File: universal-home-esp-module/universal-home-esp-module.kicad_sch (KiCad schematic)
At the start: 12 parts, among them J1 ES8311 CODEC, J10 ESP32_RPINS, J2 LDR MOD, J3 RELAYS, J4 RGB LED, J5 ENV SENSOR, J6 5V PWR, J7 EXT_GPIO, J8 EXT_I2C, J9 ESP32_LPINS, U1 ESP32-C3_SUPERMINI_SMD, U2 74HC595

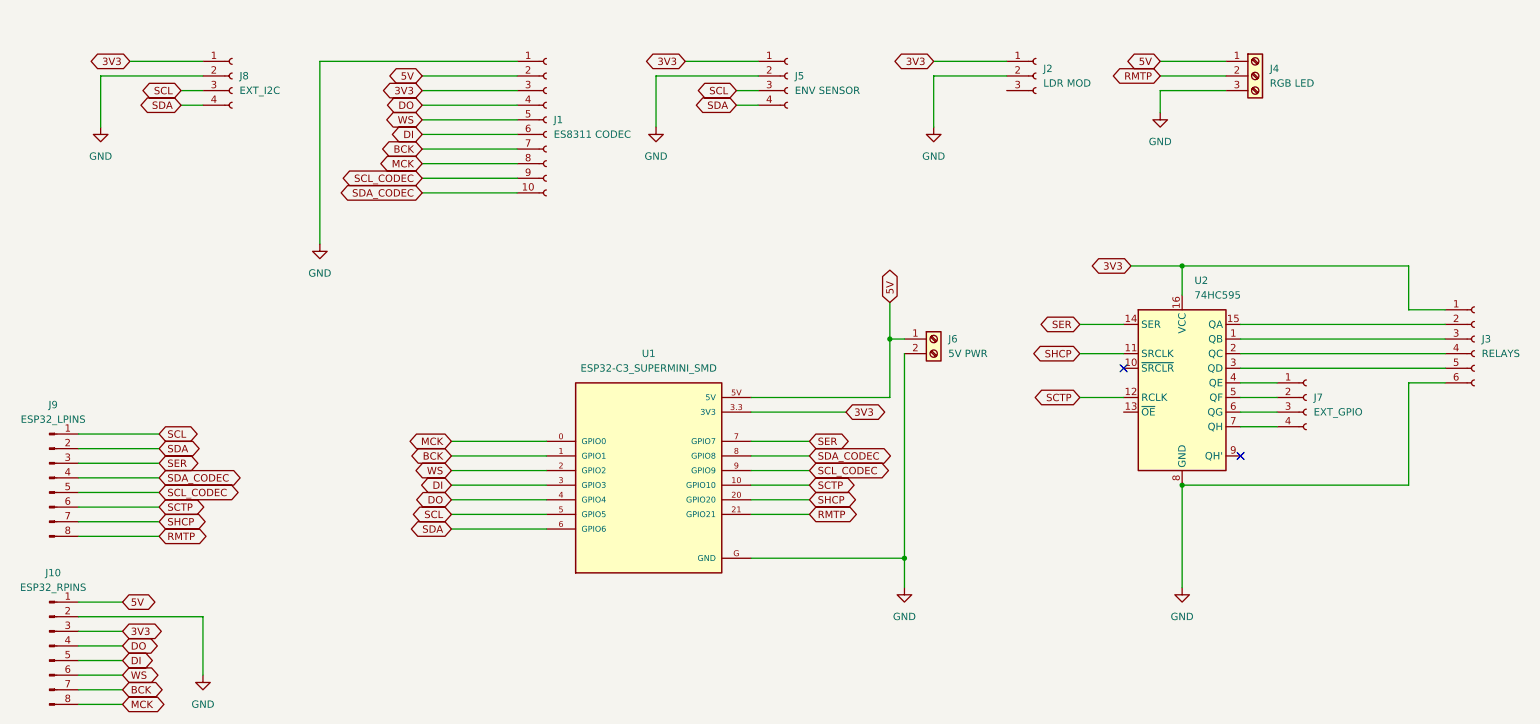
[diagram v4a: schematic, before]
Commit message: update schematic
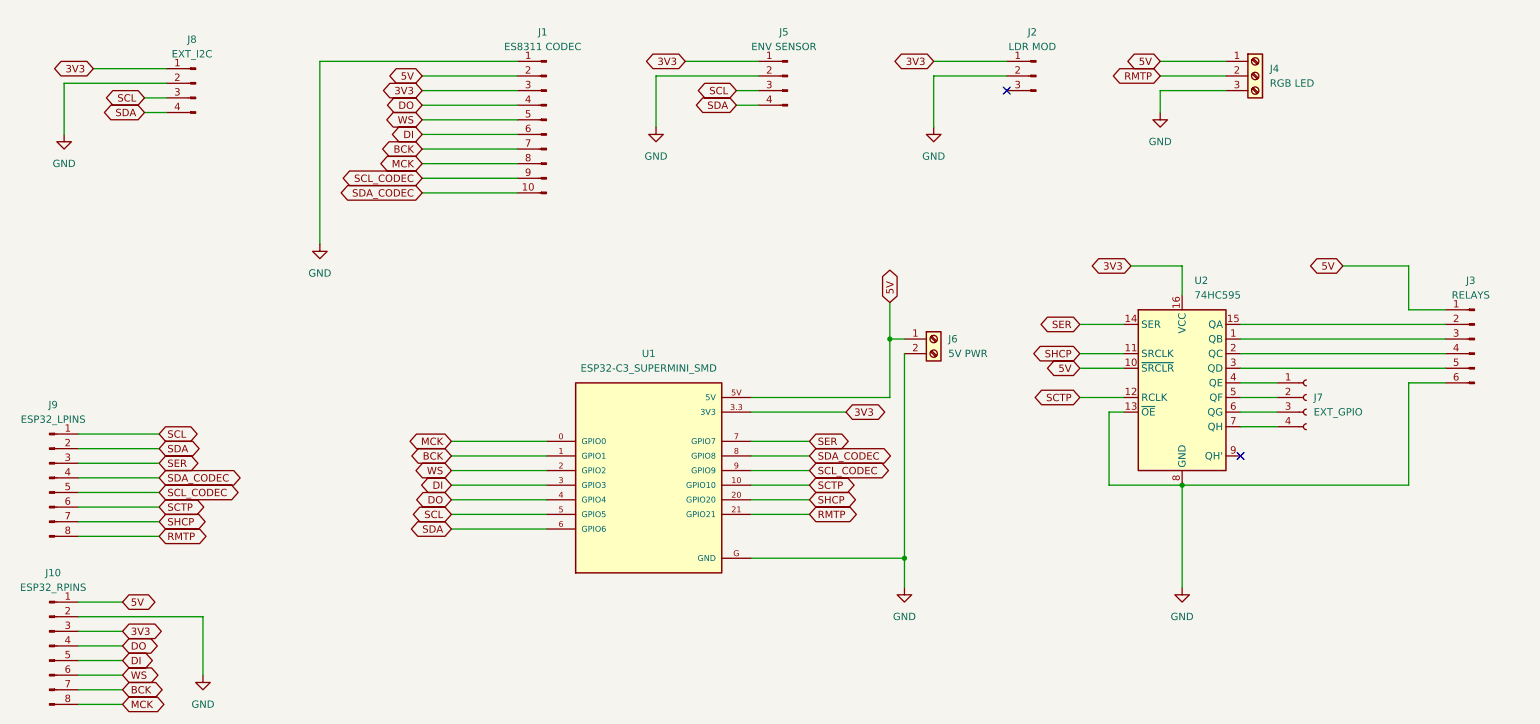
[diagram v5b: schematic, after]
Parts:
- J1: symbol Connector:Conn_01x10_Socket -> Connector:Conn_01x10_Pin
- J10, J9: footprint Connector_PinSocket_2.54mm:PinSocket_1x08_P2.54mm_Vertical -> Connector_PinHeader_2.54mm:PinHeader_1x08_P2.54mm_Vertical
- J2: footprint Connector_PinSocket_2.54mm:PinSocket_1x03_P2.54mm_Vertical -> Connector_PinHeader_2.54mm:PinHeader_1x03_P2.54mm_Vertical; symbol Connector:Conn_01x03_Socket -> Connector:Conn_01x03_Pin
- J3: footprint Connector_PinSocket_2.54mm:PinSocket_1x06_P2.54mm_Vertical -> Connector_PinHeader_2.54mm:PinHeader_1x06_P2.54mm_Vertical; symbol Connector:Conn_01x06_Socket -> Connector:Conn_01x06_Pin
- J5, J8: symbol Connector:Conn_01x04_Socket -> Connector:Conn_01x04_Pin
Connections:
- net 3V3: no longer J3.1 (Pin_1)
- net 5V: now also J3.1 (Pin_1), U2.10 (~{SRCLR})
- net GND: now also U2.13 (~{OE})
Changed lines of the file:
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@@
 	)
 	(junction
-		(at 223.52 58.42)
-		(diameter 0)
-		(color 0 0 0 0)
-	)
-	(junction
 		(at 223.52 96.52)
 		(diameter 0)
@@
 	)
 	(no_connect
-		(at 233.68 91.44)
+		(at 193.04 27.94)
 	)
 	(no_connect
-		(at 213.36 76.2)
+		(at 233.68 91.44)
 	)
 	(wire
@@
 	(wire
 		(pts
-			(xy 49.53 30.48) (xy 53.34 30.48)
+			(xy 43.18 31.75) (xy 46.99 31.75)
 		)
 		(stroke
@@
 	(wire
 		(pts
-			(xy 40.64 22.86) (xy 53.34 22.86)
+			(xy 34.29 24.13) (xy 46.99 24.13)
 		)
 		(stroke
@@
 	(wire
 		(pts
-			(xy 35.56 25.4) (xy 53.34 25.4)
+			(xy 29.21 26.67) (xy 46.99 26.67)
 		)
 		(stroke
@@
 	(wire
 		(pts
-			(xy 262.89 58.42) (xy 223.52 58.42)
+			(xy 262.89 58.42) (xy 251.46 58.42)
 		)
 		(stroke
@@
 	(wire
 		(pts
+			(xy 210.82 96.52) (xy 223.52 96.52)
+		)
+		(stroke
+			(width 0)
+			(type default)
+		)
+	)
+	(wire
+		(pts
 			(xy 148.59 91.44) (xy 158.75 91.44)
 		)
@@
 	(wire
 		(pts
+			(xy 210.82 83.82) (xy 210.82 96.52)
+		)
+		(stroke
+			(width 0)
+			(type default)
+		)
+	)
+	(wire
+		(pts
 			(xy 96.52 104.14) (xy 113.03 104.14)
 		)
@@
 	(wire
 		(pts
-			(xy 35.56 25.4) (xy 35.56 34.29)
+			(xy 213.36 83.82) (xy 210.82 83.82)
+		)
+		(stroke
+			(width 0)
+			(type default)
+		)
+	)
+	(wire
+		(pts
+			(xy 29.21 26.67) (xy 29.21 35.56)
 		)
 		(stroke
@@
 	(wire
 		(pts
+			(xy 213.36 76.2) (xy 205.74 76.2)
+		)
+		(stroke
+			(width 0)
+			(type default)
+		)
+	)
+	(wire
+		(pts
 			(xy 148.59 101.6) (xy 158.75 101.6)
 		)
@@
 	(wire
 		(pts
-			(xy 49.53 27.94) (xy 53.34 27.94)
+			(xy 43.18 29.21) (xy 46.99 29.21)
 		)
 		(stroke
@@
 	(global_label "SDA"
 		(shape bidirectional)
-		(at 49.53 30.48 180)
+		(at 43.18 31.75 180)
 		(fields_autoplaced yes)
 		(effects
@@
 		)
 		(property "Intersheetrefs" "${INTERSHEET_REFS}"
-			(at 41.8654 30.48 0)
+			(at 35.5154 31.75 0)
 			(effects
 				(font
@@
 	(global_label "SCL"
 		(shape bidirectional)
-		(at 49.53 27.94 180)
-		(fields_autoplaced yes)
+		(at 43.18 29.21 180)
 		(effects
 			(font
@@
 		)
 		(property "Intersheetrefs" "${INTERSHEET_REFS}"
-			(at 41.9259 27.94 0)
+			(at 3.8259 50.8 0)
 			(effects
 				(font
@@
 	(global_label "3V3"
 		(shape bidirectional)
-		(at 40.64 22.86 180)
-		(fields_autoplaced yes)
+		(at 34.29 24.13 180)
 		(effects
 			(font
@@
 		)
 		(property "Intersheetrefs" "${INTERSHEET_REFS}"
-			(at 33.0359 22.86 0)
+			(at -5.0641 45.72 0)
 			(effects
 				(font
@@
 		)
 	)
+	(global_label "5V"
+		(shape bidirectional)
+		(at 205.74 76.2 180)
+		(fields_autoplaced yes)
+		(effects
+			(font
+				(size 1.27 1.27)
+			)
+			(justify right)
+		)
+		(property "Intersheetrefs" "${INTERSHEET_REFS}"
+			(at 199.3454 76.2 0)
+			(effects
+				(font
+					(size 1.27 1.27)
+				)
+				(justify right)
+				(hide yes)
+			)
+		)
+	)
 	(global_label "WS"
 		(shape bidirectional)
@@
 		)
 	)
+	(global_label "5V"
+		(shape bidirectional)
+		(at 251.46 58.42 180)
+		(fields_autoplaced yes)
+		(effects
+			(font
+				(size 1.27 1.27)
+			)
+			(justify right)
+		)
+		(property "Intersheetrefs" "${INTERSHEET_REFS}"
+			(at 245.0654 58.42 0)
+			(effects
+				(font
+					(size 1.27 1.27)
+				)
+				(justify right)
+				(hide yes)
+			)
+		)
+	)
 	(global_label "SCL"
 		(shape bidirectional)
@@
 	)
 	(symbol
-		(lib_id "Connector:Conn_01x10_Socket")
+		(lib_id "Connector:Conn_01x10_Pin")
 		(at 113.03 33.02 0)
+		(mirror y)
 		(unit 1)
 		(exclude_from_sim no)
@@
 		(on_board yes)
 		(dnp no)
-		(fields_autoplaced yes)
 		(property "Reference" "J1"
-			(at 114.3 33.0199 0)
+			(at 112.395 17.78 0)
 			(effects
 				(font
 					(size 1.27 1.27)
 				)
-				(justify left)
 			)
 		)
 		(property "Value" "ES8311 CODEC"
-			(at 114.3 35.5599 0)
+			(at 112.395 20.32 0)
 			(effects
 				(font
 					(size 1.27 1.27)
 				)
-				(justify left)
 			)
 		)
@@
 			)
 		)
-		(property "Footprint" "Connector_PinSocket_2.54mm:PinSocket_1x08_P2.54mm_Vertical"
+		(property "Footprint" "Connector_PinHeader_2.54mm:PinHeader_1x08_P2.54mm_Vertical"
 			(at 26.67 95.25 0)
 			(effects
@@
 	(symbol
 		(lib_id "power:GND")
-		(at 35.56 34.29 0)
+		(at 29.21 35.56 0)
 		(unit 1)
 		(exclude_from_sim no)
@@
 		(fields_autoplaced yes)
 		(property "Reference" "#PWR07"
-			(at 35.56 40.64 0)
+			(at 29.21 41.91 0)
 			(effects
 				(font
@@
 		)
 		(property "Value" "GND"
-			(at 35.56 39.37 0)
+			(at 29.21 40.64 0)
 			(effects
 				(font
@@
 		)
 		(property "Footprint" ""
-			(at 35.56 34.29 0)
+			(at 29.21 35.56 0)
 			(effects
 				(font
@@
 		)
 		(property "Datasheet" ""
-			(at 35.56 34.29 0)
+			(at 29.21 35.56 0)
 			(effects
 				(font
@@
 		)
 		(property "Description" "Power symbol creates a global label with name \"GND\" , ground"
-			(at 35.56 34.29 0)
+			(at 29.21 35.56 0)
 			(effects
 				(font
@@
 	)
 	(symbol
-		(lib_id "Connector:Conn_01x03_Socket")
+		(lib_id "Connector:Conn_01x03_Pin")
 		(at 198.12 25.4 0)
+		(mirror y)
 		(unit 1)
 		(exclude_from_sim no)
@@
 		(on_board yes)
 		(dnp no)
-		(fields_autoplaced yes)
 		(property "Reference" "J2"
-			(at 199.39 24.1299 0)
+			(at 197.485 17.78 0)
 			(effects
 				(font
 					(size 1.27 1.27)
 				)
-				(justify left)
 			)
 		)
 		(property "Value" "LDR MOD"
-			(at 199.39 26.6699 0)
+			(at 197.485 20.32 0)
 			(effects
 				(font
 					(size 1.27 1.27)
 				)
-				(justify left)
 			)
 		)
-		(property "Footprint" "Connector_PinSocket_2.54mm:PinSocket_1x03_P2.54mm_Vertical"
+		(property "Footprint" "Connector_PinHeader_2.54mm:PinHeader_1x03_P2.54mm_Vertical"
 			(at 198.12 25.4 0)
 			(effects
@@
 			)
 		)
-		(property "Footprint" "Connector_PinSocket_2.54mm:PinSocket_1x08_P2.54mm_Vertical"
+		(property "Footprint" "Connector_PinHeader_2.54mm:PinHeader_1x08_P2.54mm_Vertical"
 			(at 26.67 124.46 0)
 			(effects
@@
 	)
 	(symbol
-		(lib_id "Connector:Conn_01x04_Socket")
+		(lib_id "Connector:Conn_01x04_Pin")
 		(at 154.94 25.4 0)
+		(mirror y)
 		(unit 1)
 		(exclude_from_sim no)
@@
 		(on_board yes)
 		(dnp no)
-		(fields_autoplaced yes)
 		(property "Reference" "J5"
-			(at 156.21 25.3999 0)
+			(at 154.305 17.78 0)
 			(effects
 				(font
 					(size 1.27 1.27)
 				)
-				(justify left)
 			)
 		)
 		(property "Value" "ENV SENSOR"
-			(at 156.21 27.9399 0)
+			(at 154.305 20.32 0)
 			(effects
 				(font
 					(size 1.27 1.27)
 				)
-				(justify left)
 			)
 		)
@@
 	)
 	(symbol
-		(lib_id "Connector:Conn_01x06_Socket")
+		(lib_id "Connector:Conn_01x06_Pin")
 		(at 274.32 71.12 0)
+		(mirror y)
 		(unit 1)
 		(exclude_from_sim no)
@@
 		(on_board yes)
 		(dnp no)
-		(fields_autoplaced yes)
 		(property "Reference" "J3"
-			(at 275.59 71.1199 0)
+			(at 273.685 60.96 0)
 			(effects
 				(font
 					(size 1.27 1.27)
 				)
-				(justify left)
 			)
 		)
 		(property "Value" "RELAYS"
-			(at 275.59 73.6599 0)
+			(at 273.685 63.5 0)
 			(effects
 				(font
 					(size 1.27 1.27)
 				)
-				(justify left)
 			)
 		)
-		(property "Footprint" "Connector_PinSocket_2.54mm:PinSocket_1x06_P2.54mm_Vertical"
+		(property "Footprint" "Connector_PinHeader_2.54mm:PinHeader_1x06_P2.54mm_Vertical"
 			(at 274.32 71.12 0)
 			(effects
@@
 	)
 	(symbol
-		(lib_id "Connector:Conn_01x04_Socket")
-		(at 58.42 25.4 0)
+		(lib_id "Connector:Conn_01x04_Pin")
+		(at 52.07 26.67 0)
+		(mirror y)
 		(unit 1)
 		(exclude_from_sim no)
@@
 		(on_board yes)
 		(dnp no)
-		(fields_autoplaced yes)
 		(property "Reference" "J8"
-			(at 59.69 25.3999 0)
+			(at 51.435 19.05 0)
 			(effects
 				(font
 					(size 1.27 1.27)
 				)
-				(justify left)
 			)
 		)
 		(property "Value" "EXT_I2C"
-			(at 59.69 27.9399 0)
+			(at 51.435 21.59 0)
 			(effects
 				(font
 					(size 1.27 1.27)
 				)
-				(justify left)
 			)
 		)
 		(property "Footprint" "Connector_PinHeader_2.54mm:PinHeader_1x04_P2.54mm_Vertical"
-			(at 58.42 25.4 0)
+			(at 52.07 26.67 0)
 			(effects
 				(font
@@
 		)
 		(property "Datasheet" "~"
-			(at 58.42 25.4 0)
+			(at 52.07 26.67 0)
 			(effects
 				(font
@@
 		)
 		(property "Description" "Generic connector, single row, 01x04, script generated"
-			(at 58.42 25.4 0)
+			(at 52.07 26.67 0)
 			(effects
 				(font
